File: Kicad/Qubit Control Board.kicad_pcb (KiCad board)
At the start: 6 copper layers, 64 x 81.5 mm, 147 parts, among them J1 USB_C_Receptacle_PowerOnly_6P, J2 CLK_Pins, J3 Idata, J4 Qdata, J5 SPIdata, J6 SMA, U1 LT3045xMSE, U2 TRF372017IRGZR, U3 LT3045xMSE, U4 LT3045xMSE, U5 SN65LVDS1DBV, U6 AD9743BCPZ, Y1 SiT8008xx-3x-xxN, Y2 CVHD-950-100.000

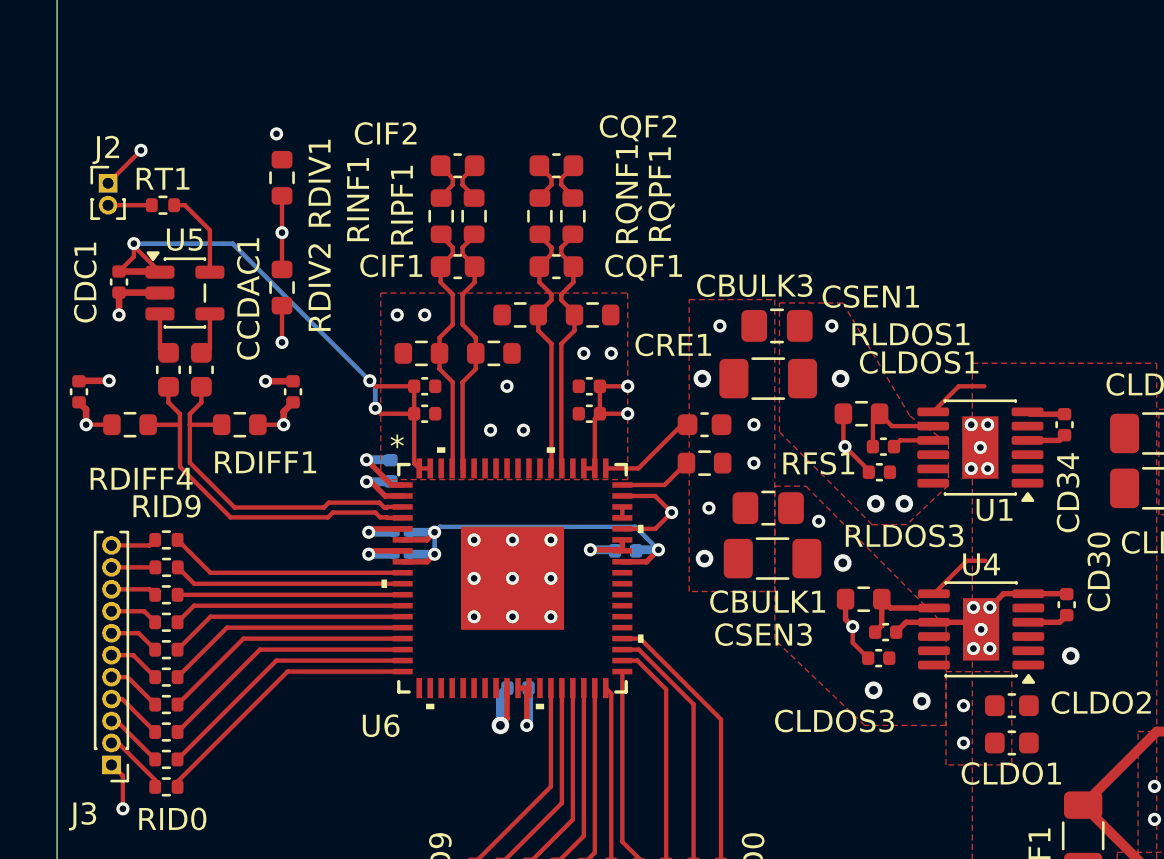
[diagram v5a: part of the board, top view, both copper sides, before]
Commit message: added 3.3V decoupling cap for DAC to the bottom
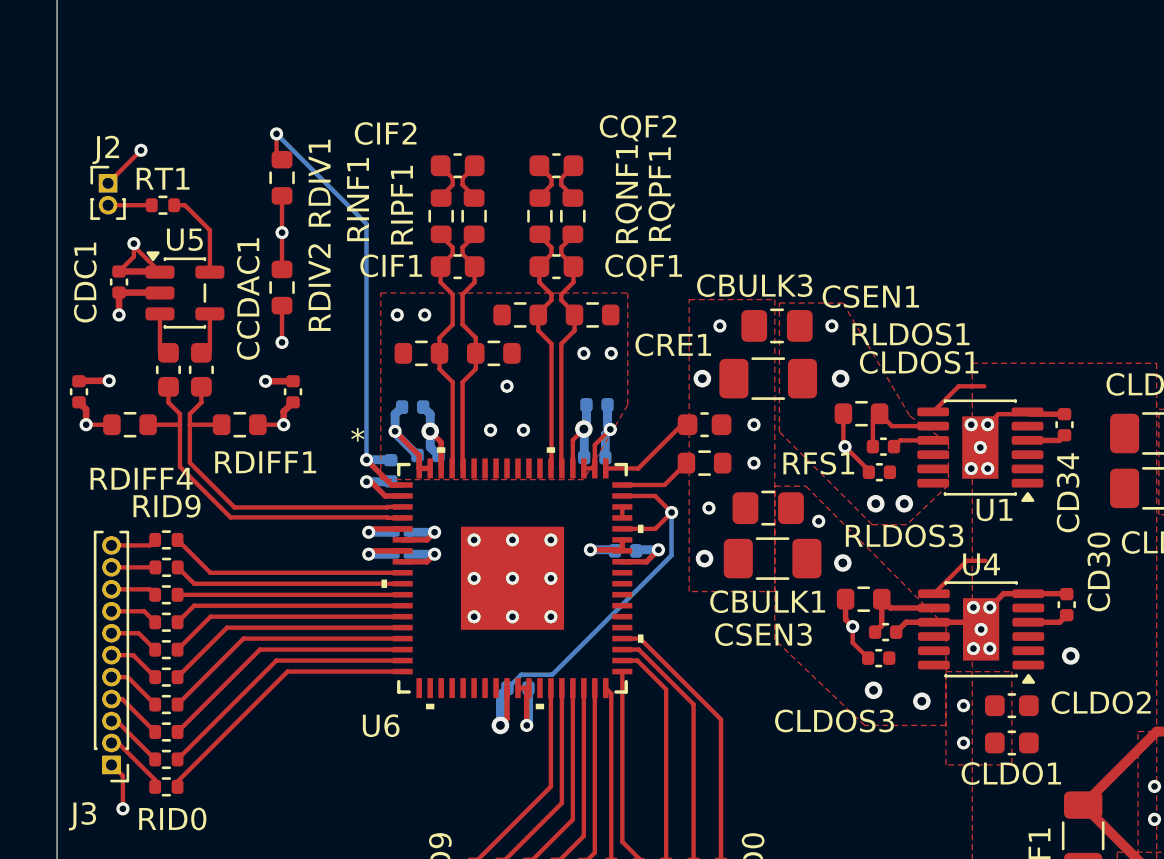
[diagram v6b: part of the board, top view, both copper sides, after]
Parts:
- CD6, CD7, CD8, CD9: moved to B.Cu
- moved CD6 3.15 mm to (123.4, 92.9)
- moved CD8 2.02 mm to (131.0, 93.0)
- moved CD9 0.92 mm to (131.1, 90.6)
- moved CD7 0.63 mm to (122.7, 90.7)
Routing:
- net GND: track 52.7 -> 63.6 mm, vias 62 -> 64
- net +1.8V: track 23.6 -> 29.7 mm
- net +3.3V-A: track 43.9 -> 38.3 mm, vias 11 -> 9

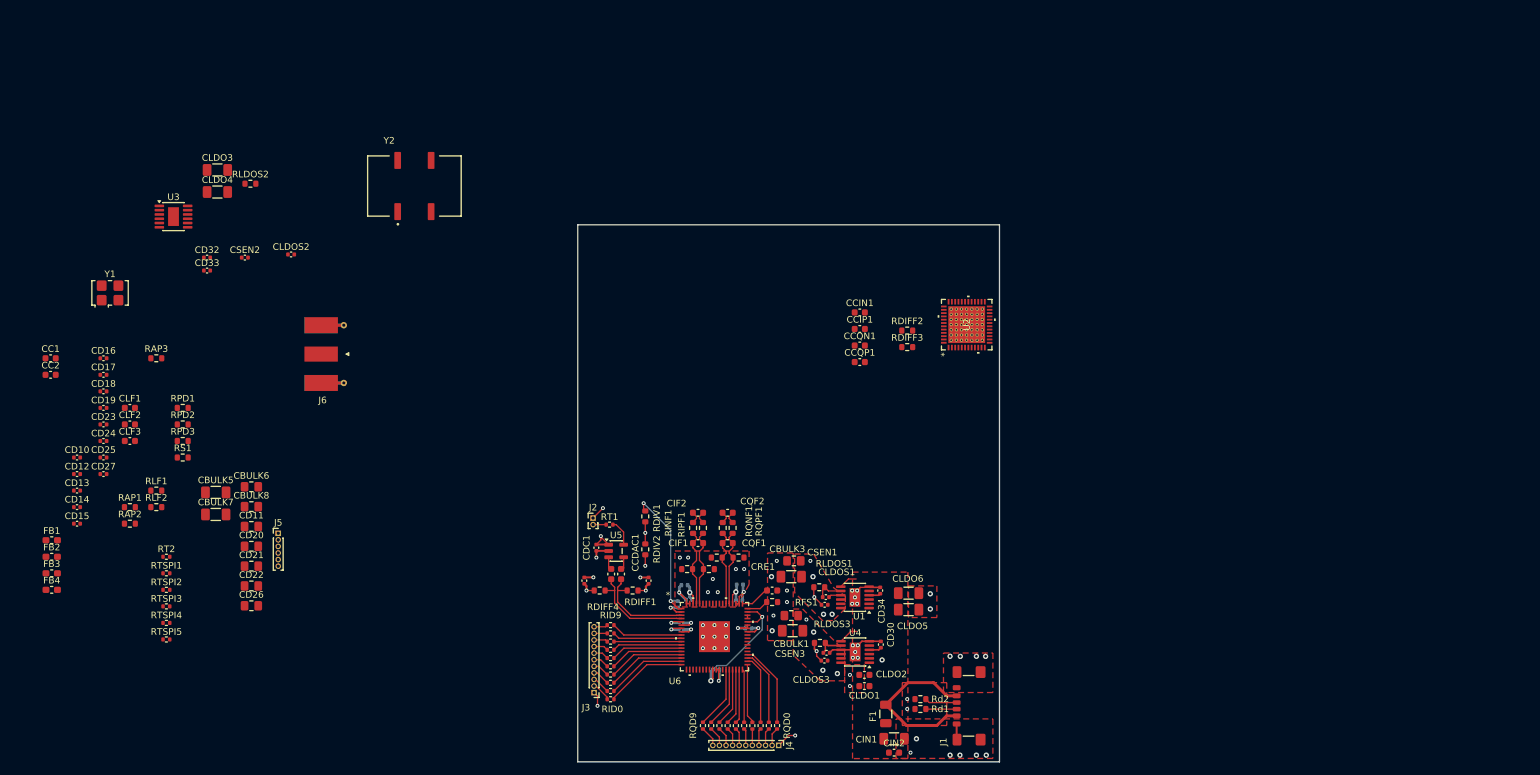
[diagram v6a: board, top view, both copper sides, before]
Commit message: added extra F beads to PLL power input
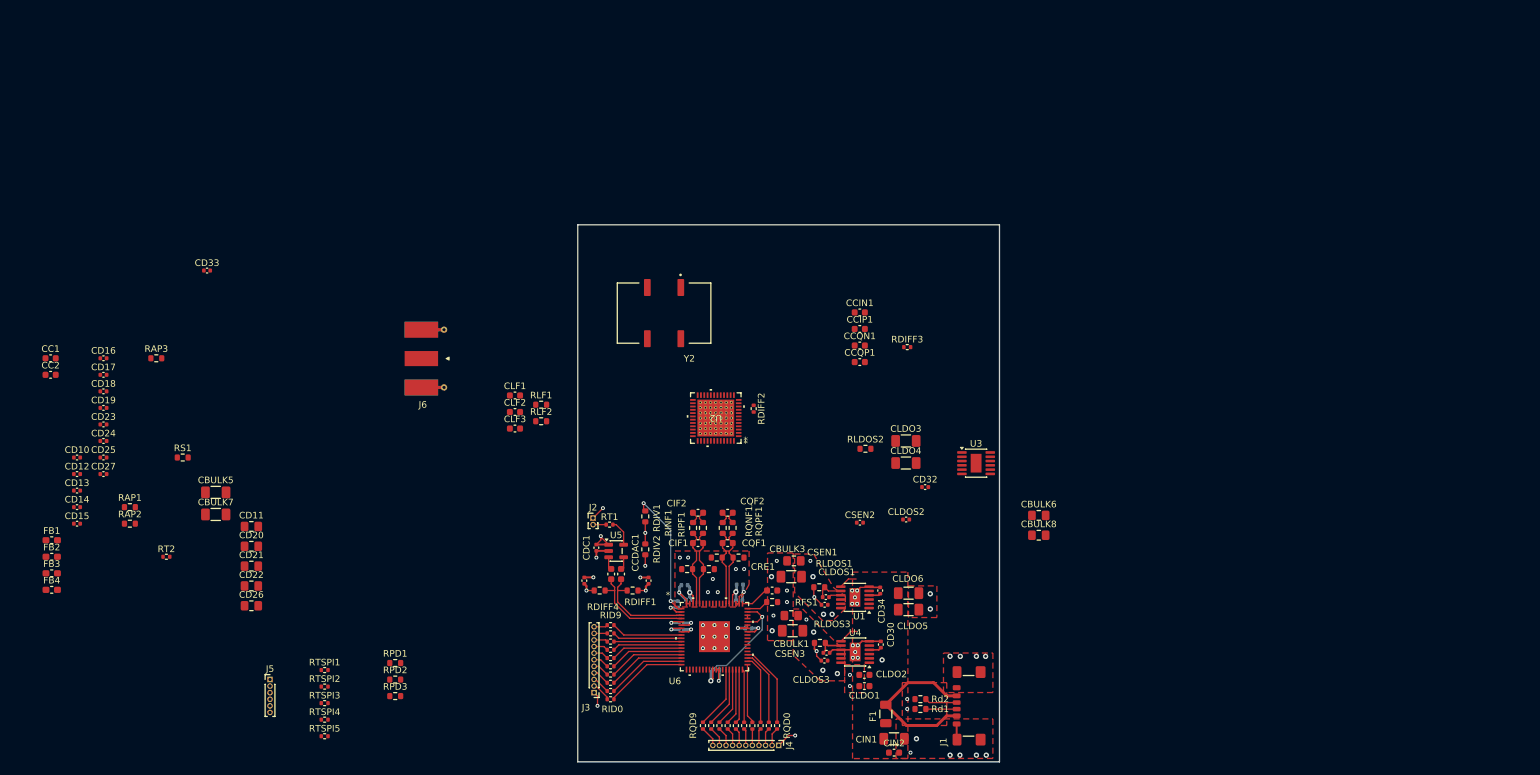
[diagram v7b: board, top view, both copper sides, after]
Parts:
- removed Y1: SiT8008xx-3x-xxN, Oscillator:Oscillator_SMD_SiT_PQFN-4Pin_5.0x3.2mm
- RDIFF2, RDIFF3: footprint Resistor_SMD:R_0603_1608Metric -> Resistor_SMD:R_0402_1005Metric
- moved U3 127.4 mm to (166.9, 72.2)
- moved CBULK6 119.6 mm to (176.5, 80.1)
- moved CBULK8 119.6 mm to (176.5, 83.1)
- moved CD32 114.4 mm to (159.2, 75.8)
- moved CLDO3 112.3 mm to (156.3, 68.8)
- moved CLDO4 112.3 mm to (156.3, 72.2)
- moved CLDOS2 101.6 mm to (156.3, 80.7)
- moved CSEN2 101.6 mm to (149.3, 81.2)
- moved RLDOS2 101.6 mm to (150.2, 70.0)
- moved RLF1 59.8 mm to (101.0, 63.3)
- moved RLF2 59.8 mm to (101.0, 65.8)
- moved CLF1 58.5 mm to (97.0, 61.9)
- moved CLF2 58.5 mm to (97.0, 64.4)
- moved CLF3 58.5 mm to (97.0, 66.9)
- moved RPD1 50.4 mm to (78.8, 102.5)
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
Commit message: LF edits and cap resizing
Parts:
- added FB5: 1k @100MHz, Inductor_SMD:L_0603_1608Metric_Pad1.05x0.95mm_HandSolder, F.Cu at (22.5, 83.9)
- added FB6: 1k @100MHz, Inductor_SMD:L_0603_1608Metric_Pad1.05x0.95mm_HandSolder, F.Cu at (22.5, 86.4)
- added FB7: 1k @100MHz, Inductor_SMD:L_0603_1608Metric_Pad1.05x0.95mm_HandSolder, F.Cu at (22.5, 88.9)
- added FB8: 1k @100MHz, Inductor_SMD:L_0603_1608Metric_Pad1.05x0.95mm_HandSolder, F.Cu at (22.5, 91.4)
- CD2, CD3: footprint Capacitor_SMD:C_0201_0603Metric -> Capacitor_SMD:C_0402_1005Metric
- CLF1, CLF2, CLF3: footprint Capacitor_SMD:C_0603_1608Metric -> Capacitor_SMD:C_0402_1005Metric
- RLF1, RLF2: footprint Resistor_SMD:R_0603_1608Metric -> Resistor_SMD:R_0402_1005Metric
- moved RDIFF3 35.0 mm to (122.1, 61.0), turned to -90 degrees
- moved CCIN1 31.9 mm to (119.9, 61.8)
- moved CCIP1 30.6 mm to (119.9, 60.2)
- moved CLF1 30.2 mm to (126.3, 69.0)
- moved CLF2 30.0 mm to (126.3, 70.9)
- moved CCQN1 16.6 mm to (134.5, 61.8), turned to 180 degrees
- moved CCQP1 15.2 mm to (134.5, 60.2), turned to 180 degrees
- moved RLF1 3.35 mm to (100.4, 66.6)
- moved RLF2 3.35 mm to (100.4, 69.1)
- moved CLF3 3.35 mm to (96.4, 70.2)
- moved RDIFF2 3.04 mm to (132.3, 61.0)
- moved U2 2.86 mm to (127.2, 62.5)
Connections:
- CD12 pad 2: Net-(U2-VCC_D2S) -> /VCC_D2S
- CD13 pad 2: Net-(U2-VCC_D2S) -> /VCC_MIX
- CD14 pad 2: Net-(U2-VCC_D2S) -> /VCC_D2S
- CD15 pad 2: Net-(U2-VCC_D2S) -> /VCC_MIX
- CD16 pad 2: /VCC_LO1 -> /VCC_LO2
- CD18 pad 2: /VCC_LO1 -> /VCC_LO2
- CD21 pad 2: /VCC_PLL -> /VCC_VCO1
- CD22 pad 2: /VCC_PLL -> /VCC_VCO2
- CD24 pad 2: /VCC_PLL -> /VCC_VCO1
- CD25 pad 2: /VCC_PLL -> /VCC_VCO2
- FB1 pad 2: Net-(U2-VCC_D2S) -> /VCC_D2S
- FB2 pad 2: /VCC_LO1 -> /VCC_LO2
- U2 pad 20: Net-(U2-VCC_D2S) -> /VCC_D2S
- U2 pad 21: Net-(U2-VCC_D2S) -> /VCC_MIX
- U2 pad 30: /VCC_LO1 -> /VCC_LO2
- U2 pad 32: /VCC_PLL -> /VCC_VCO2
- U2 pad 35: /VCC_PLL -> /VCC_VCO1
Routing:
- net /BBQP: track 2.02 -> 24.3 mm
- net /BBIP: track 2.02 -> 24.2 mm
- net /BBQN: track 2.02 -> 22.7 mm
- net /BBIN: track 2.02 -> 22.6 mm
- net Net-(U2-BBI_N): track 0.00 -> 3.29 mm
- net Net-(U2-BBQ_N): track 0.00 -> 3.29 mm
- net Net-(U2-BBI_P): track 0.00 -> 3.27 mm
- net Net-(U2-BBQ_P): track 0.00 -> 3.27 mm
